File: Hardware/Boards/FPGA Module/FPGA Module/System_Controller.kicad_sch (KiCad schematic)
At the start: 30 parts, among them SW1 RST, U7 W25Q16JVUXIQ TR, U8 RP2040, Y1 12Mhz

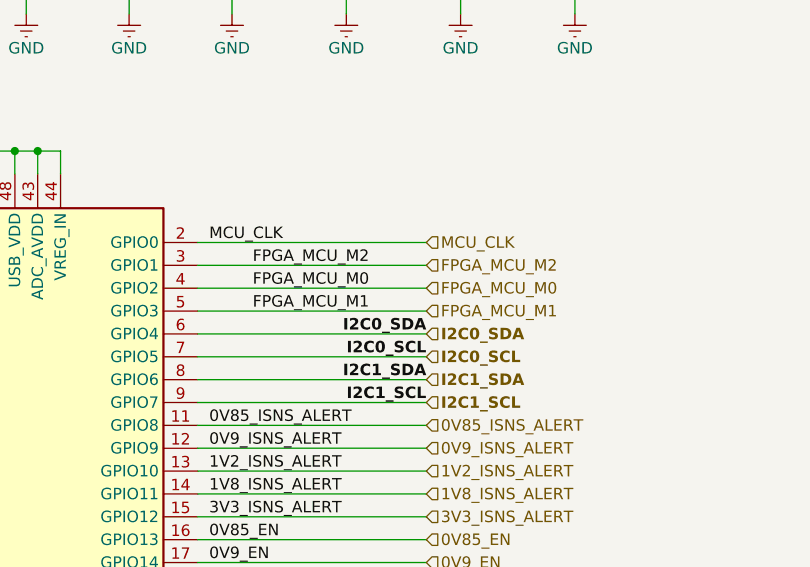
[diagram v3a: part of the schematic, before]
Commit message: Updated DDR4 routing
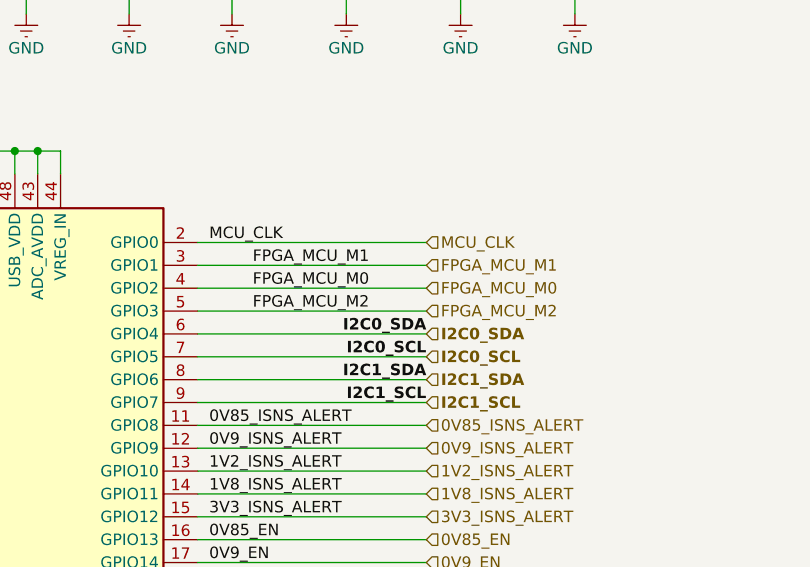
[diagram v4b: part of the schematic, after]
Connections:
- net FPGA_MCU_M1: now also U8.3 (GPIO1); no longer U8.5 (GPIO3)
- net FPGA_MCU_M2: now also U8.5 (GPIO3); no longer U8.3 (GPIO1)
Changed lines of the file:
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@@
-		)
-	)
-	(label "FPGA_MCU_M1"
-		(at 237.49 124.46 180)
-		(fields_autoplaced yes)
-		(effects
-			(font
-				(size 1.27 1.27)
-			)
-			(justify right bottom)
 		)
 	)
@@
 		)
 	)
-	(label "FPGA_MCU_M2"
+	(label "FPGA_MCU_M1"
 		(at 237.49 119.38 180)
 		(fields_autoplaced yes)
@@
 		)
 	)
+	(label "FPGA_MCU_M2"
+		(at 237.49 124.46 180)
+		(fields_autoplaced yes)
+		(effects
+			(font
+				(size 1.27 1.27)
+			)
+			(justify right bottom)
+		)
+	)
 	(label "SYS_SPI_MISO"
 		(at 219.71 157.48 0)
@@
 		)
 	)
+	(hierarchical_label "0V9_EN"
+		(shape input)
+		(at 243.84 152.4 0)
+		(fields_autoplaced yes)
+		(effects
+			(font
+				(size 1.27 1.27)
+			)
+			(justify left)
+		)
+	)
+	(hierarchical_label "1V2_ISNS_ALERT"
+		(shape input)
+		(at 243.84 142.24 0)
+		(fields_autoplaced yes)
+		(effects
+			(font
+				(size 1.27 1.27)
+			)
+			(justify left)
+		)
+	)
+	(hierarchical_label "LVL_SHIFT_EN"
+		(shape input)
+		(at 243.84 175.26 0)
+		(fields_autoplaced yes)
+		(effects
+			(font
+				(size 1.27 1.27)
+			)
+			(justify left)
+		)
+	)
+	(hierarchical_label "FPGA_MCU_M1"
+		(shape input)
+		(at 243.84 119.38 0)
+		(fields_autoplaced yes)
+		(effects
+			(font
+				(size 1.27 1.27)
+			)
+			(justify left)
+		)
+	)
+	(hierarchical_label "0V85_ISNS_ALERT"
+		(shape input)
+		(at 243.84 137.16 0)
+		(fields_autoplaced yes)
+		(effects
+			(font
+				(size 1.27 1.27)
+			)
+			(justify left)
+		)
+	)
+	(hierarchical_label "I2C1_SDA"
+		(shape input)
+		(at 243.84 132.08 0)
+		(fields_autoplaced yes)
+		(effects
+			(font
+				(size 1.27 1.27)
+				(bold yes)
+			)
+			(justify left)
+		)
+	)
+	(hierarchical_label "SYS_SPI_CS"
+		(shape input)
+		(at 243.84 160.02 0)
+		(fields_autoplaced yes)
+		(effects
+			(font
+				(size 1.27 1.27)
+			)
+			(justify left)
+		)
+	)
+	(hierarchical_label "I2C0_SDA"
+		(shape input)
+		(at 243.84 127 0)
+		(fields_autoplaced yes)
+		(effects
+			(font
+				(size 1.27 1.27)
+				(bold yes)
+			)
+			(justify left)
+		)
+	)
+	(hierarchical_label "3V3_AON"
+		(shape input)
+		(at 269.24 81.28 0)
+		(fields_autoplaced yes)
+		(effects
+			(font
+				(size 1.27 1.27)
+			)
+			(justify left)
+		)
+	)
+	(hierarchical_label "1V8_EN"
+		(shape input)
+		(at 243.84 167.64 0)
+		(fields_autoplaced yes)
+		(effects
+			(font
+				(size 1.27 1.27)
+			)
+			(justify left)
+		)
+	)
+	(hierarchical_label "0V9_ISNS_ALERT"
+		(shape input)
+		(at 243.84 139.7 0)
+		(fields_autoplaced yes)
+		(effects
+			(font
+				(size 1.27 1.27)
+			)
+			(justify left)
+		)
+	)
+	(hierarchical_label "1V2_EN"
+		(shape input)
+		(at 243.84 154.94 0)
+		(fields_autoplaced yes)
+		(effects
+			(font
+				(size 1.27 1.27)
+			)
+			(justify left)
+		)
+	)
+	(hierarchical_label "3V3_EN"
+		(shape input)
+		(at 243.84 172.72 0)
+		(fields_autoplaced yes)
+		(effects
+			(font
+				(size 1.27 1.27)
+			)
+			(justify left)
+		)
+	)
+	(hierarchical_label "FPGA_MCU_M0"
+		(shape input)
+		(at 243.84 121.92 0)
+		(fields_autoplaced yes)
+		(effects
+			(font
+				(size 1.27 1.27)
+			)
+			(justify left)
+		)
+	)
+	(hierarchical_label "2V5_EN"
+		(shape input)
+		(at 243.84 170.18 0)
+		(fields_autoplaced yes)
+		(effects
+			(font
+				(size 1.27 1.27)
+			)
+			(justify left)
+		)
+	)
+	(hierarchical_label "1V8_ISNS_ALERT"
+		(shape input)
+		(at 243.84 144.78 0)
+		(fields_autoplaced yes)
+		(effects
+			(font
+				(size 1.27 1.27)
+			)
+			(justify left)
+		)
+	)
+	(hierarchical_label "USB_SYSMON_D_N"
+		(shape input)
+		(at 147.32 127 180)
+		(fields_autoplaced yes)
+		(effects
+			(font
+				(size 1.27 1.27)
+			)
+			(justify right)
+		)
+	)
+	(hierarchical_label "USB_SYSMON_D_P"
+		(shape input)
+		(at 147.32 124.46 180)
+		(fields_autoplaced yes)
+		(effects
+			(font
+				(size 1.27 1.27)
+			)
+			(justify right)
+		)
+	)
 	(hierarchical_label "FPGA_MCU_M2"
 		(shape input)
-		(at 243.84 119.38 0)
-		(fields_autoplaced yes)
-		(effects
-			(font
-				(size 1.27 1.27)
-			)
-			(justify left)
-		)
-	)
-	(hierarchical_label "0V9_EN"
-		(shape input)
-		(at 243.84 152.4 0)
-		(fields_autoplaced yes)
-		(effects
-			(font
-				(size 1.27 1.27)
-			)
-			(justify left)
-		)
-	)
-	(hierarchical_label "1V2_ISNS_ALERT"
-		(shape input)
-		(at 243.84 142.24 0)
-		(fields_autoplaced yes)
-		(effects
-			(font
-				(size 1.27 1.27)
-			)
-			(justify left)
-		)
-	)
-	(hierarchical_label "LVL_SHIFT_EN"
-		(shape input)
-		(at 243.84 175.26 0)
-		(fields_autoplaced yes)
-		(effects
-			(font
-				(size 1.27 1.27)
-			)
-			(justify left)
-		)
-	)
-	(hierarchical_label "0V85_ISNS_ALERT"
-		(shape input)
-		(at 243.84 137.16 0)
-		(fields_autoplaced yes)
-		(effects
-			(font
-				(size 1.27 1.27)
-			)
-			(justify left)
-		)
-	)
-	(hierarchical_label "I2C1_SDA"
-		(shape input)
-		(at 243.84 132.08 0)
-		(fields_autoplaced yes)
-		(effects
-			(font
-				(size 1.27 1.27)
-				(bold yes)
-			)
-			(justify left)
-		)
-	)
-	(hierarchical_label "SYS_SPI_CS"
-		(shape input)
-		(at 243.84 160.02 0)
-		(fields_autoplaced yes)
-		(effects
-			(font
-				(size 1.27 1.27)
-			)
-			(justify left)
-		)
-	)
-	(hierarchical_label "I2C0_SDA"
-		(shape input)
-		(at 243.84 127 0)
-		(fields_autoplaced yes)
-		(effects
-			(font
-				(size 1.27 1.27)
-				(bold yes)
-			)
-			(justify left)
-		)
-	)
-	(hierarchical_label "3V3_AON"
-		(shape input)
-		(at 269.24 81.28 0)
-		(fields_autoplaced yes)
-		(effects
-			(font
-				(size 1.27 1.27)
-			)
-			(justify left)
-		)
-	)
-	(hierarchical_label "1V8_EN"
-		(shape input)
-		(at 243.84 167.64 0)
-		(fields_autoplaced yes)
-		(effects
-			(font
-				(size 1.27 1.27)
-			)
-			(justify left)
-		)
-	)
-	(hierarchical_label "0V9_ISNS_ALERT"
-		(shape input)
-		(at 243.84 139.7 0)
-		(fields_autoplaced yes)
-		(effects
-			(font
-				(size 1.27 1.27)
-			)
-			(justify left)
-		)
-	)
-	(hierarchical_label "1V2_EN"
-		(shape input)
-		(at 243.84 154.94 0)
-		(fields_autoplaced yes)
-		(effects
-			(font
-				(size 1.27 1.27)
-			)
-			(justify left)
-		)
-	)
-	(hierarchical_label "FPGA_MCU_M1"
-		(shape input)
 		(at 243.84 124.46 0)
 		(fields_autoplaced yes)
@@
 		)
 	)
-	(hierarchical_label "3V3_EN"
-		(shape input)
-		(at 243.84 172.72 0)
-		(fields_autoplaced yes)
-		(effects
-			(font
-				(size 1.27 1.27)
-			)
-			(justify left)
-		)
-	)
-	(hierarchical_label "FPGA_MCU_M0"
-		(shape input)
-		(at 243.84 121.92 0)
-		(fields_autoplaced yes)
-		(effects
-			(font
-				(size 1.27 1.27)
-			)
-			(justify left)
-		)
-	)
-	(hierarchical_label "2V5_EN"
-		(shape input)
-		(at 243.84 170.18 0)
-		(fields_autoplaced yes)
-		(effects
-			(font
-				(size 1.27 1.27)
-			)
-			(justify left)
-		)
-	)
-	(hierarchical_label "1V8_ISNS_ALERT"
-		(shape input)
-		(at 243.84 144.78 0)
-		(fields_autoplaced yes)
-		(effects
-			(font
-				(size 1.27 1.27)
-			)
-			(justify left)
-		)
-	)
-	(hierarchical_label "USB_SYSMON_D_N"
-		(shape input)
-		(at 147.32 127 180)
-		(fields_autoplaced yes)
-		(effects
-			(font
-				(size 1.27 1.27)
-			)
-			(justify right)
-		)
-	)
-	(hierarchical_label "USB_SYSMON_D_P"
-		(shape input)
-		(at 147.32 124.46 180)
-		(fields_autoplaced yes)
-		(effects
-			(font
-				(size 1.27 1.27)
-			)
-			(justify right)
-		)
-	)

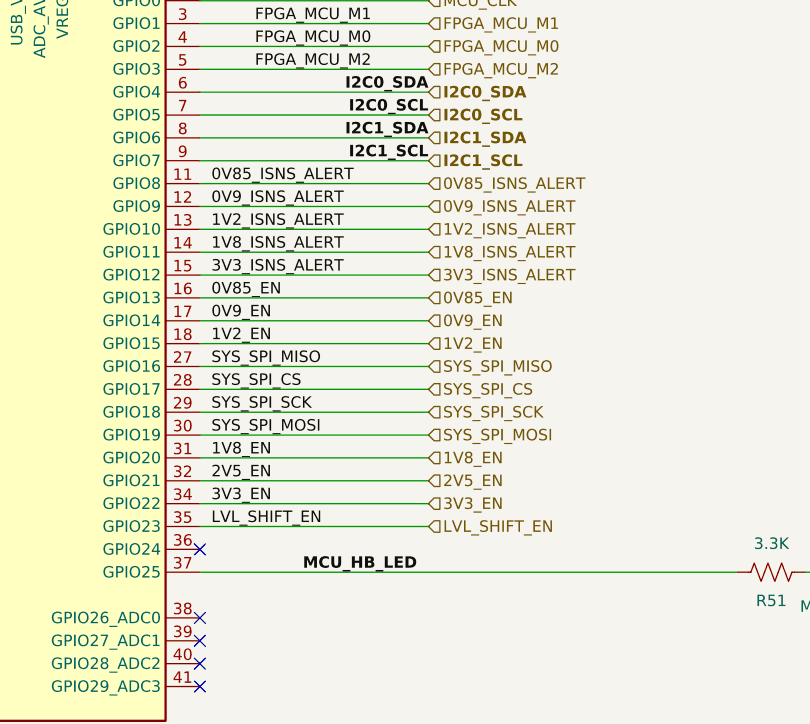
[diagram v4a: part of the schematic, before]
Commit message: Completed FPGA Module Layout
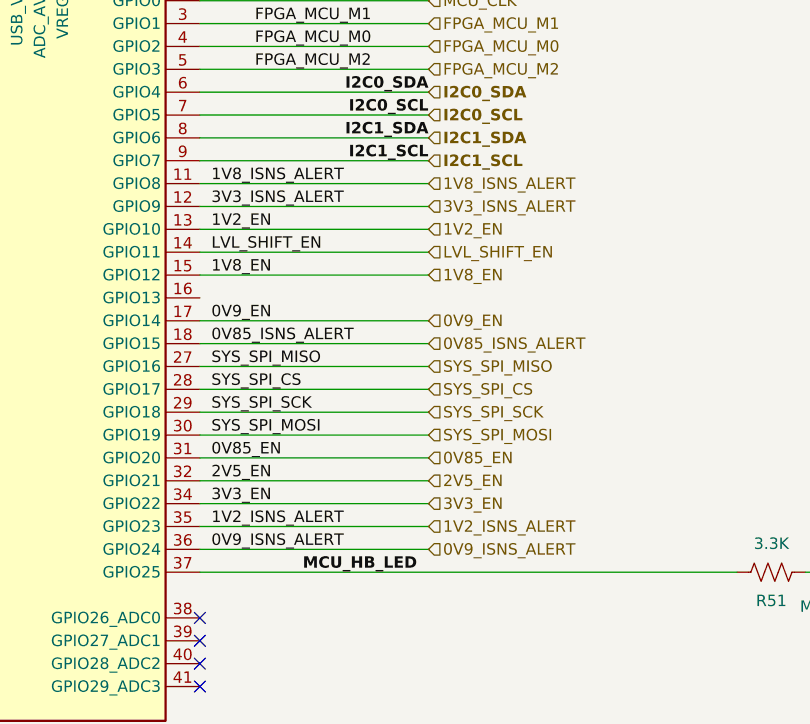
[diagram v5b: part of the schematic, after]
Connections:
- net 0V85_EN: now also U8.31 (GPIO20); no longer U8.16 (GPIO13)
- net 0V85_ISNS_ALERT: now also U8.18 (GPIO15); no longer U8.11 (GPIO8)
- net 0V9_ISNS_ALERT: now also U8.36 (GPIO24); no longer U8.12 (GPIO9)
- net 1V2_EN: now also U8.13 (GPIO10); no longer U8.18 (GPIO15)
- net 1V2_ISNS_ALERT: now also U8.35 (GPIO23); no longer U8.13 (GPIO10)
- net 1V8_EN: now also U8.15 (GPIO12); no longer U8.31 (GPIO20)
- net 1V8_ISNS_ALERT: now also U8.11 (GPIO8); no longer U8.14 (GPIO11)
- net 3V3_ISNS_ALERT: now also U8.12 (GPIO9); no longer U8.15 (GPIO12)
- net LVL_SHIFT_EN: now also U8.14 (GPIO11); no longer U8.35 (GPIO23)
- no-connect marks 6 -> 5

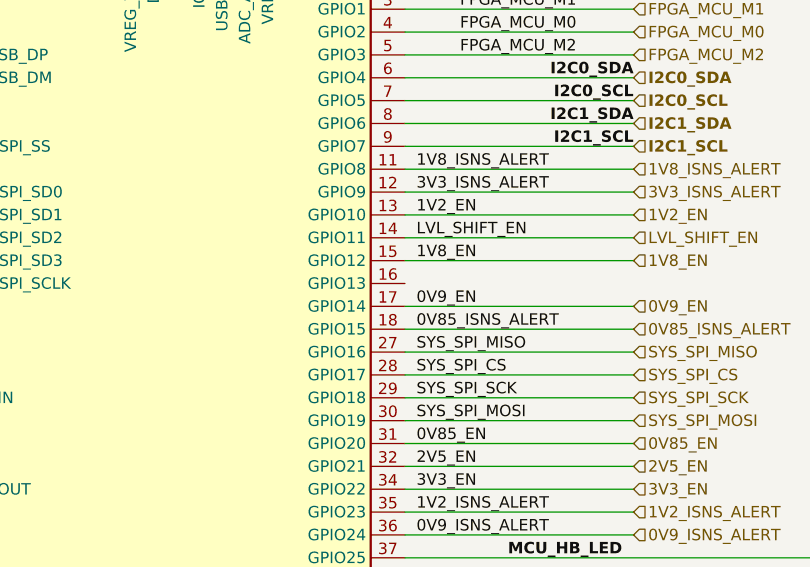
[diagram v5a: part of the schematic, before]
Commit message: Fixed FPGA Module Routing
Reversed B2B headers and re-routed connections to FPGA
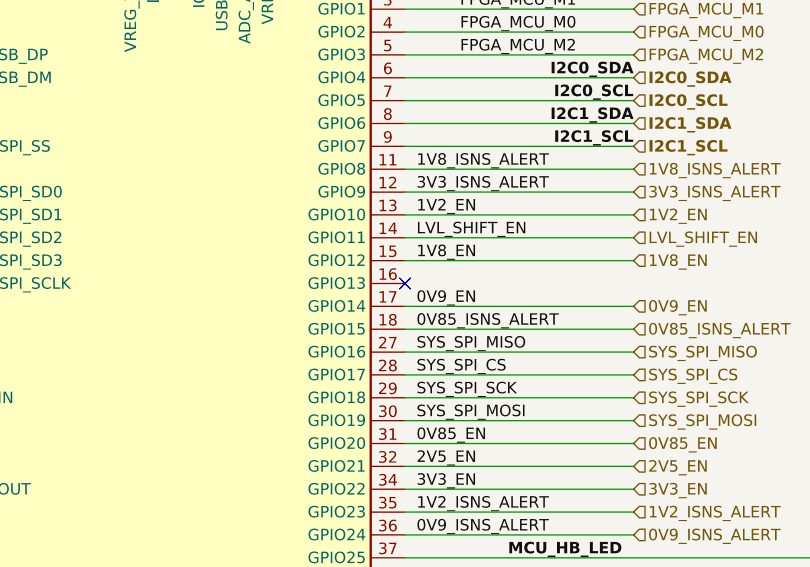
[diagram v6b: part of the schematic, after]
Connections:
- no-connect marks 5 -> 6
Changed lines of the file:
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@@
+	)
+	(no_connect
+		(at 218.44 149.86)
 	)
 	(no_connect

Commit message: Generated FPGA module gerbers
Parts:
- TP21, TP22, TP23, TP24, TP25, TP26, TP27: footprint FPGA Module:Test Point 0.75mm -> FPGA Module:Test Point 0.5mm No Silk
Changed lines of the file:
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@@
 			)
 		)
-		(property "Footprint" "FPGA Module:Test Point 0.75mm"
+		(property "Footprint" "FPGA Module:Test Point 0.5mm No Silk"
 			(at 149.86 213.36 0)
 			(effects
@@
 			)
 		)
-		(property "Footprint" "FPGA Module:Test Point 0.75mm"
+		(property "Footprint" "FPGA Module:Test Point 0.5mm No Silk"
 			(at 149.86 210.82 0)
 			(effects
@@
 			)
 		)
-		(property "Footprint" "FPGA Module:Test Point 0.75mm"
+		(property "Footprint" "FPGA Module:Test Point 0.5mm No Silk"
 			(at 160.02 180.34 0)
 			(effects
@@
 			)
 		)
-		(property "Footprint" "FPGA Module:Test Point 0.75mm"
+		(property "Footprint" "FPGA Module:Test Point 0.5mm No Silk"
 			(at 149.86 215.9 0)
 			(effects
@@
 			)
 		)
-		(property "Footprint" "FPGA Module:Test Point 0.75mm"
+		(property "Footprint" "FPGA Module:Test Point 0.5mm No Silk"
 			(at 149.86 208.28 0)
 			(effects
@@
 			)
 		)
-		(property "Footprint" "FPGA Module:Test Point 0.75mm"
+		(property "Footprint" "FPGA Module:Test Point 0.5mm No Silk"
 			(at 193.04 80.01 0)
 			(effects
@@
 			)
 		)
-		(property "Footprint" "FPGA Module:Test Point 0.75mm"
+		(property "Footprint" "FPGA Module:Test Point 0.5mm No Silk"
 			(at 160.02 177.8 0)
 			(effects
